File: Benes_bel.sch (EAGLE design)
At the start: 27 parts, among them J1 DCJ0202, K1 HE751, K2 HE751, K3 HE751, K4 HE751, T1 BC337, T2 BC337, T3 BC337, T4 BC337, X5 FH12-08S-1SH

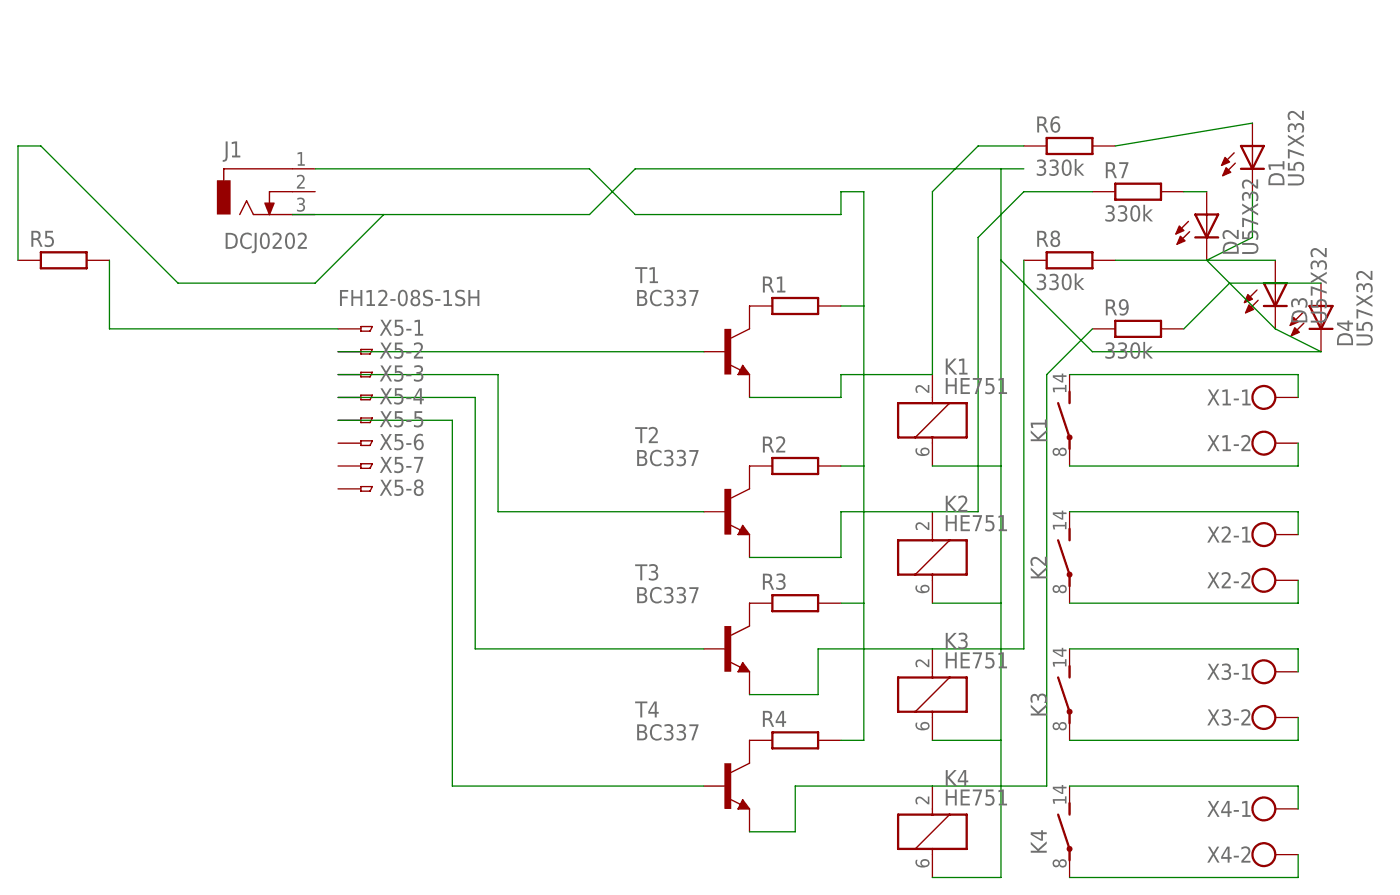
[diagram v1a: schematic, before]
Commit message: Bord werkt op eerste pcb ontbreken 3 draden in de schema's en de prod files is dit aangepast.
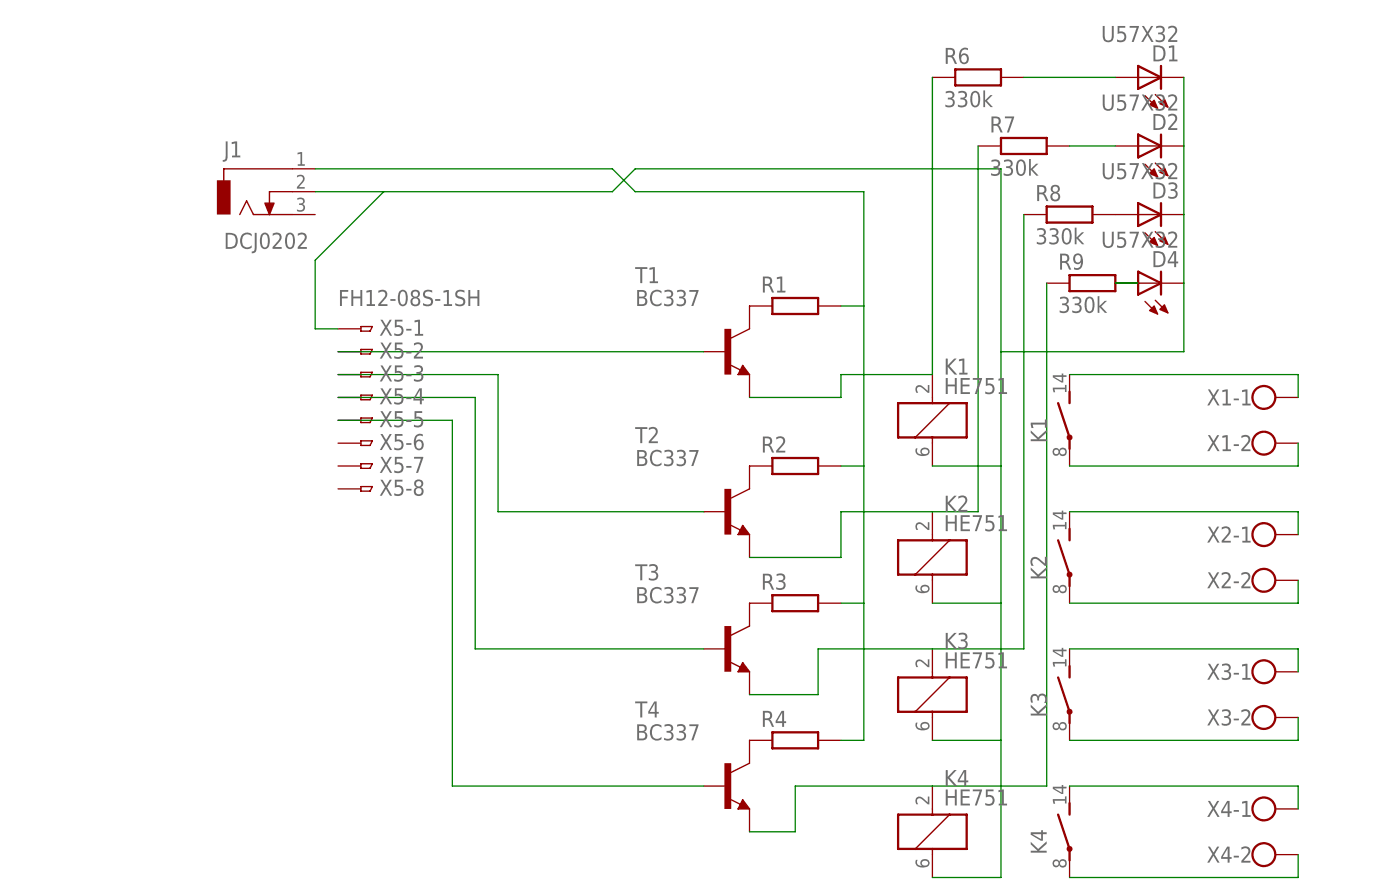
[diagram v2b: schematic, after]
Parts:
- removed R5: (no value), resistor:R-EU_0207/12
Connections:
- removed net N$22: R5.2, X5-1.1
- removed net N$28: D1.C, D2.C, D3.C, D4.C, K11.2, K21.2, K31.2, K41.2, R5.1
- removed net N$30: R8.1
- new net N$21: D1.C, D2.C, D3.C, D4.C, J1.2, K11.2, K21.2, K31.2, K41.2, X5-1.1
- net N$19: now also R8.1
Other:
- moved on the sheet: D1, D2, D3, D4, R6, R7, R8, R9
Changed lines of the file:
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@@
 <part name="X5" library="con-hirose" deviceset="FH12-08S-1S" device="H"/>
 <part name="J1" library="con-jack" deviceset="DCJ0202" device=""/>
-<part name="R5" library="resistor" deviceset="R-EU_" device="0207/12"/>
 <part name="R6" library="resistor" deviceset="R-EU_" device="0207/12" value="330k"/>
 <part name="R7" library="resistor" deviceset="R-EU_" device="0207/12" value="330k"/>
-<part name="R8" library="resistor" deviceset="R-EU_" device="0207/12" value="330k"/>
 <part name="R9" library="resistor" deviceset="R-EU_" device="0207/12" value="330k"/>
 <part name="D1" library="led" deviceset="U57X32" device=""/>
@@
 <part name="D3" library="led" deviceset="U57X32" device=""/>
 <part name="D4" library="led" deviceset="U57X32" device=""/>
+<part name="R8" library="resistor" deviceset="R-EU_" device="0207/12" value="330k"/>
 </parts>
 <sheets>
@@
 <instance part="X5" gate="-8" x="10.16" y="78.74"/>
 <instance part="J1" gate="G$1" x="-2.54" y="111.76"/>
-<instance part="R5" gate="G$1" x="-22.86" y="104.14"/>
-<instance part="R6" gate="G$1" x="88.9" y="116.84"/>
-<instance part="R7" gate="G$1" x="96.52" y="111.76"/>
-<instance part="R8" gate="G$1" x="88.9" y="104.14"/>
-<instance part="R9" gate="G$1" x="96.52" y="96.52"/>
-<instance part="D1" gate="1" x="109.22" y="116.84"/>
-<instance part="D2" gate="1" x="104.14" y="109.22"/>
-<instance part="D3" gate="1" x="111.76" y="101.6"/>
-<instance part="D4" gate="1" x="116.84" y="99.06"/>
+<instance part="R6" gate="G$1" x="78.74" y="124.46"/>
+<instance part="R7" gate="G$1" x="83.82" y="116.84"/>
+<instance part="R9" gate="G$1" x="91.44" y="101.6"/>
+<instance part="D1" gate="1" x="96.52" y="124.46" rot="R90"/>
+<instance part="D2" gate="1" x="96.52" y="116.84" rot="R90"/>
+<instance part="D3" gate="1" x="96.52" y="109.22" rot="R90"/>
+<instance part="D4" gate="1" x="96.52" y="101.6" rot="R90"/>
+<instance part="R8" gate="G$1" x="88.9" y="109.22"/>
 </instances>
 <busses>
@@
 <pinref part="R4" gate="G$1" pin="2"/>
 <wire x1="66.04" y1="50.8" x2="63.5" y2="50.8" width="0.1524" layer="91"/>
-<wire x1="63.5" y1="109.22" x2="63.5" y2="111.76" width="0.1524" layer="91"/>
-<wire x1="63.5" y1="111.76" x2="66.04" y2="111.76" width="0.1524" layer="91"/>
-<wire x1="63.5" y1="109.22" x2="40.64" y2="109.22" width="0.1524" layer="91"/>
-<wire x1="40.64" y1="109.22" x2="35.56" y2="114.3" width="0.1524" layer="91"/>
 <pinref part="J1" gate="G$1" pin="1"/>
-<wire x1="35.56" y1="114.3" x2="5.08" y2="114.3" width="0.1524" layer="91"/>
+<wire x1="5.08" y1="114.3" x2="38.1" y2="114.3" width="0.1524" layer="91"/>
+<wire x1="38.1" y1="114.3" x2="40.64" y2="111.76" width="0.1524" layer="91"/>
+<wire x1="40.64" y1="111.76" x2="66.04" y2="111.76" width="0.1524" layer="91"/>
 </segment>
 </net>
@@
 <wire x1="63.5" y1="88.9" x2="53.34" y2="88.9" width="0.1524" layer="91"/>
 <pinref part="R6" gate="G$1" pin="1"/>
-<wire x1="83.82" y1="116.84" x2="78.74" y2="116.84" width="0.1524" layer="91"/>
-<wire x1="78.74" y1="116.84" x2="73.66" y2="111.76" width="0.1524" layer="91"/>
-<wire x1="73.66" y1="111.76" x2="73.66" y2="91.44" width="0.1524" layer="91"/>
+<wire x1="73.66" y1="124.46" x2="73.66" y2="91.44" width="0.1524" layer="91"/>
 </segment>
 </net>
@@
 <wire x1="63.5" y1="71.12" x2="53.34" y2="71.12" width="0.1524" layer="91"/>
 <pinref part="R7" gate="G$1" pin="1"/>
-<wire x1="91.44" y1="111.76" x2="83.82" y2="111.76" width="0.1524" layer="91"/>
-<wire x1="83.82" y1="111.76" x2="78.74" y2="106.68" width="0.1524" layer="91"/>
-<wire x1="78.74" y1="106.68" x2="78.74" y2="76.2" width="0.1524" layer="91"/>
+<wire x1="78.74" y1="116.84" x2="78.74" y2="76.2" width="0.1524" layer="91"/>
 <wire x1="78.74" y1="76.2" x2="73.66" y2="76.2" width="0.1524" layer="91"/>
 </segment>
@@
 <wire x1="60.96" y1="60.96" x2="60.96" y2="55.88" width="0.1524" layer="91"/>
 <wire x1="60.96" y1="55.88" x2="53.34" y2="55.88" width="0.1524" layer="91"/>
+<wire x1="73.66" y1="60.96" x2="83.82" y2="60.96" width="0.1524" layer="91"/>
+<pinref part="R8" gate="G$1" pin="1"/>
+<wire x1="83.82" y1="60.96" x2="83.82" y2="109.22" width="0.1524" layer="91"/>
 </segment>
 </net>
@@
 <wire x1="58.42" y1="40.64" x2="53.34" y2="40.64" width="0.1524" layer="91"/>
 <pinref part="R9" gate="G$1" pin="1"/>
-<wire x1="91.44" y1="96.52" x2="86.36" y2="91.44" width="0.1524" layer="91"/>
-<wire x1="86.36" y1="91.44" x2="86.36" y2="45.72" width="0.1524" layer="91"/>
+<wire x1="86.36" y1="101.6" x2="86.36" y2="45.72" width="0.1524" layer="91"/>
 <wire x1="86.36" y1="45.72" x2="73.66" y2="45.72" width="0.1524" layer="91"/>
-</segment>
-</net>
-<net name="N$22" class="0">
-<segment>
-<pinref part="X5" gate="-1" pin="1"/>
-<wire x1="7.62" y1="96.52" x2="-17.78" y2="96.52" width="0.1524" layer="91"/>
-<pinref part="R5" gate="G$1" pin="2"/>
-<wire x1="-17.78" y1="96.52" x2="-17.78" y2="104.14" width="0.1524" layer="91"/>
 </segment>
 </net>
@@
 <pinref part="D1" gate="1" pin="A"/>
 <pinref part="R6" gate="G$1" pin="2"/>
-<wire x1="109.22" y1="119.38" x2="93.98" y2="116.84" width="0.1524" layer="91"/>
+<wire x1="93.98" y1="124.46" x2="83.82" y2="124.46" width="0.1524" layer="91"/>
 </segment>
 </net>
@@
 <pinref part="D2" gate="1" pin="A"/>
 <pinref part="R7" gate="G$1" pin="2"/>
-<wire x1="104.14" y1="111.76" x2="101.6" y2="111.76" width="0.1524" layer="91"/>
-</segment>
-</net>
-<net name="N$27" class="0">
-<segment>
-<pinref part="R8" gate="G$1" pin="2"/>
-<pinref part="D3" gate="1" pin="A"/>
-<wire x1="93.98" y1="104.14" x2="111.76" y2="104.14" width="0.1524" layer="91"/>
+<wire x1="93.98" y1="116.84" x2="88.9" y2="116.84" width="0.1524" layer="91"/>
 </segment>
 </net>
@@
 <pinref part="D4" gate="1" pin="A"/>
 <pinref part="R9" gate="G$1" pin="2"/>
-<wire x1="116.84" y1="101.6" x2="106.68" y2="101.6" width="0.1524" layer="91"/>
-<wire x1="106.68" y1="101.6" x2="101.6" y2="96.52" width="0.1524" layer="91"/>
-</segment>
-</net>
-<net name="N$30" class="0">
-<segment>
-<pinref part="R8" gate="G$1" pin="1"/>
-<wire x1="83.82" y1="104.14" x2="83.82" y2="60.96" width="0.1524" layer="91"/>
-<wire x1="83.82" y1="60.96" x2="73.66" y2="60.96" width="0.1524" layer="91"/>
-</segment>
-</net>
-<net name="N$28" class="0">
-<segment>
-<pinref part="R5" gate="G$1" pin="1"/>
-<wire x1="-27.94" y1="104.14" x2="-27.94" y2="116.84" width="0.1524" layer="91"/>
-<wire x1="-27.94" y1="116.84" x2="-25.4" y2="116.84" width="0.1524" layer="91"/>
-<wire x1="-25.4" y1="116.84" x2="-10.16" y2="101.6" width="0.1524" layer="91"/>
-<wire x1="-10.16" y1="101.6" x2="5.08" y2="101.6" width="0.1524" layer="91"/>
+<wire x1="93.98" y1="101.6" x2="96.52" y2="101.6" width="0.1524" layer="91"/>
+</segment>
+</net>
+<net name="N$21" class="0">
+<segment>
+<pinref part="D4" gate="1" pin="C"/>
+<pinref part="D3" gate="1" pin="C"/>
+<pinref part="D2" gate="1" pin="C"/>
+<pinref part="D1" gate="1" pin="C"/>
+<wire x1="101.6" y1="124.46" x2="101.6" y2="116.84" width="0.1524" layer="91"/>
+<wire x1="101.6" y1="116.84" x2="101.6" y2="109.22" width="0.1524" layer="91"/>
+<wire x1="101.6" y1="109.22" x2="101.6" y2="101.6" width="0.1524" layer="91"/>
+<wire x1="101.6" y1="101.6" x2="101.6" y2="93.98" width="0.1524" layer="91"/>
 <pinref part="K4" gate="1" pin="2"/>
 <wire x1="73.66" y1="35.56" x2="81.28" y2="35.56" width="0.1524" layer="91"/>
@@
 <pinref part="K1" gate="1" pin="2"/>
 <wire x1="81.28" y1="81.28" x2="73.66" y2="81.28" width="0.1524" layer="91"/>
-<wire x1="83.82" y1="114.3" x2="81.28" y2="114.3" width="0.1524" layer="91"/>
-<wire x1="81.28" y1="114.3" x2="81.28" y2="104.14" width="0.1524" layer="91"/>
-<wire x1="81.28" y1="104.14" x2="81.28" y2="81.28" width="0.1524" layer="91"/>
-<pinref part="D1" gate="1" pin="C"/>
-<pinref part="D2" gate="1" pin="C"/>
-<wire x1="109.22" y1="111.76" x2="109.22" y2="106.68" width="0.1524" layer="91"/>
-<wire x1="109.22" y1="106.68" x2="104.14" y2="104.14" width="0.1524" layer="91"/>
-<pinref part="D3" gate="1" pin="C"/>
-<wire x1="104.14" y1="104.14" x2="111.76" y2="96.52" width="0.1524" layer="91"/>
-<pinref part="D4" gate="1" pin="C"/>
-<wire x1="111.76" y1="96.52" x2="116.84" y2="93.98" width="0.1524" layer="91"/>
-<wire x1="116.84" y1="93.98" x2="91.44" y2="93.98" width="0.1524" layer="91"/>
-<wire x1="91.44" y1="93.98" x2="81.28" y2="104.14" width="0.1524" layer="91"/>
+<wire x1="81.28" y1="114.3" x2="81.28" y2="93.98" width="0.1524" layer="91"/>
+<wire x1="81.28" y1="93.98" x2="81.28" y2="81.28" width="0.1524" layer="91"/>
 <wire x1="81.28" y1="114.3" x2="40.64" y2="114.3" width="0.1524" layer="91"/>
-<wire x1="40.64" y1="114.3" x2="35.56" y2="109.22" width="0.1524" layer="91"/>
-<wire x1="35.56" y1="109.22" x2="12.7" y2="109.22" width="0.1524" layer="91"/>
-<wire x1="12.7" y1="109.22" x2="2.54" y2="109.22" width="0.1524" layer="91"/>
-<wire x1="5.08" y1="101.6" x2="12.7" y2="109.22" width="0.1524" layer="91"/>
-</segment>
-</net>
+<wire x1="101.6" y1="93.98" x2="81.28" y2="93.98" width="0.1524" layer="91"/>
+<wire x1="38.1" y1="111.76" x2="40.64" y2="114.3" width="0.1524" layer="91"/>
+<pinref part="J1" gate="G$1" pin="2"/>
+<wire x1="5.08" y1="111.76" x2="12.7" y2="111.76" width="0.1524" layer="91"/>
+<wire x1="38.1" y1="111.76" x2="12.7" y2="111.76" width="0.1524" layer="91"/>
+<wire x1="12.7" y1="111.76" x2="5.08" y2="104.14" width="0.1524" layer="91"/>
+<pinref part="X5" gate="-1" pin="1"/>
+<wire x1="7.62" y1="96.52" x2="5.08" y2="96.52" width="0.1524" layer="91"/>
+<wire x1="5.08" y1="96.52" x2="5.08" y2="104.14" width="0.1524" layer="91"/>
+</segment>
+</net>
+<net name="N$27" class="0">
+<segment>
+<pinref part="D3" gate="1" pin="A"/>
+<pinref part="R8" gate="G$1" pin="2"/>
+</segment>
+</net>
